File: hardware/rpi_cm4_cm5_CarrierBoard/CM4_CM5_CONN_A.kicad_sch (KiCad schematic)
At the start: 60 parts, among them J19 RPI_CMx_A, J6 M20-9990245, J7 2998TR, Q12 2N7002, U19 SN74LVC1G125DBVR, U21 MCP7940NT-I/MS, Y2 32.768kHz

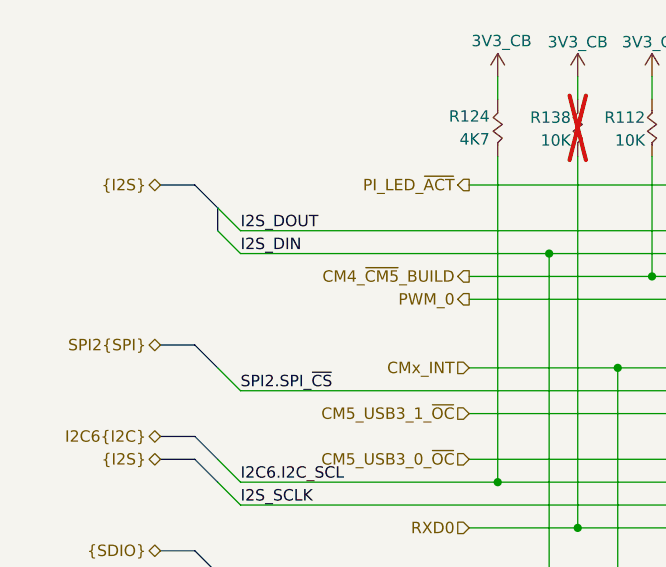
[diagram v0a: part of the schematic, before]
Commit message: Update preliminary placement, update DNP, regen BOM + Preliminary schematics
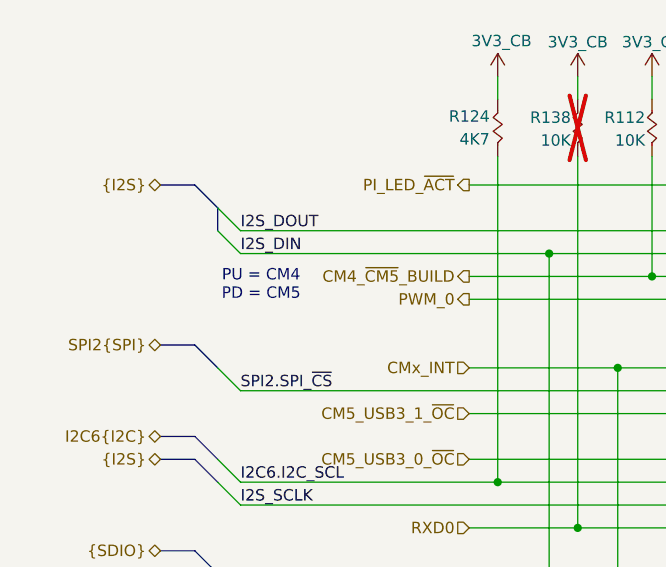
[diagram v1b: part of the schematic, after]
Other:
- note added: "PU = CM4 PD = CM5"
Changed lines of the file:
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@@
+		)
+	)
+	(text "PU = CM4\nPD = CM5"
+		(exclude_from_sim no)
+		(at 35.306 54.356 0)
+		(effects
+			(font
+				(size 1.27 1.27)
+				(color 255 153 0 1)
+			)
 		)
 	)

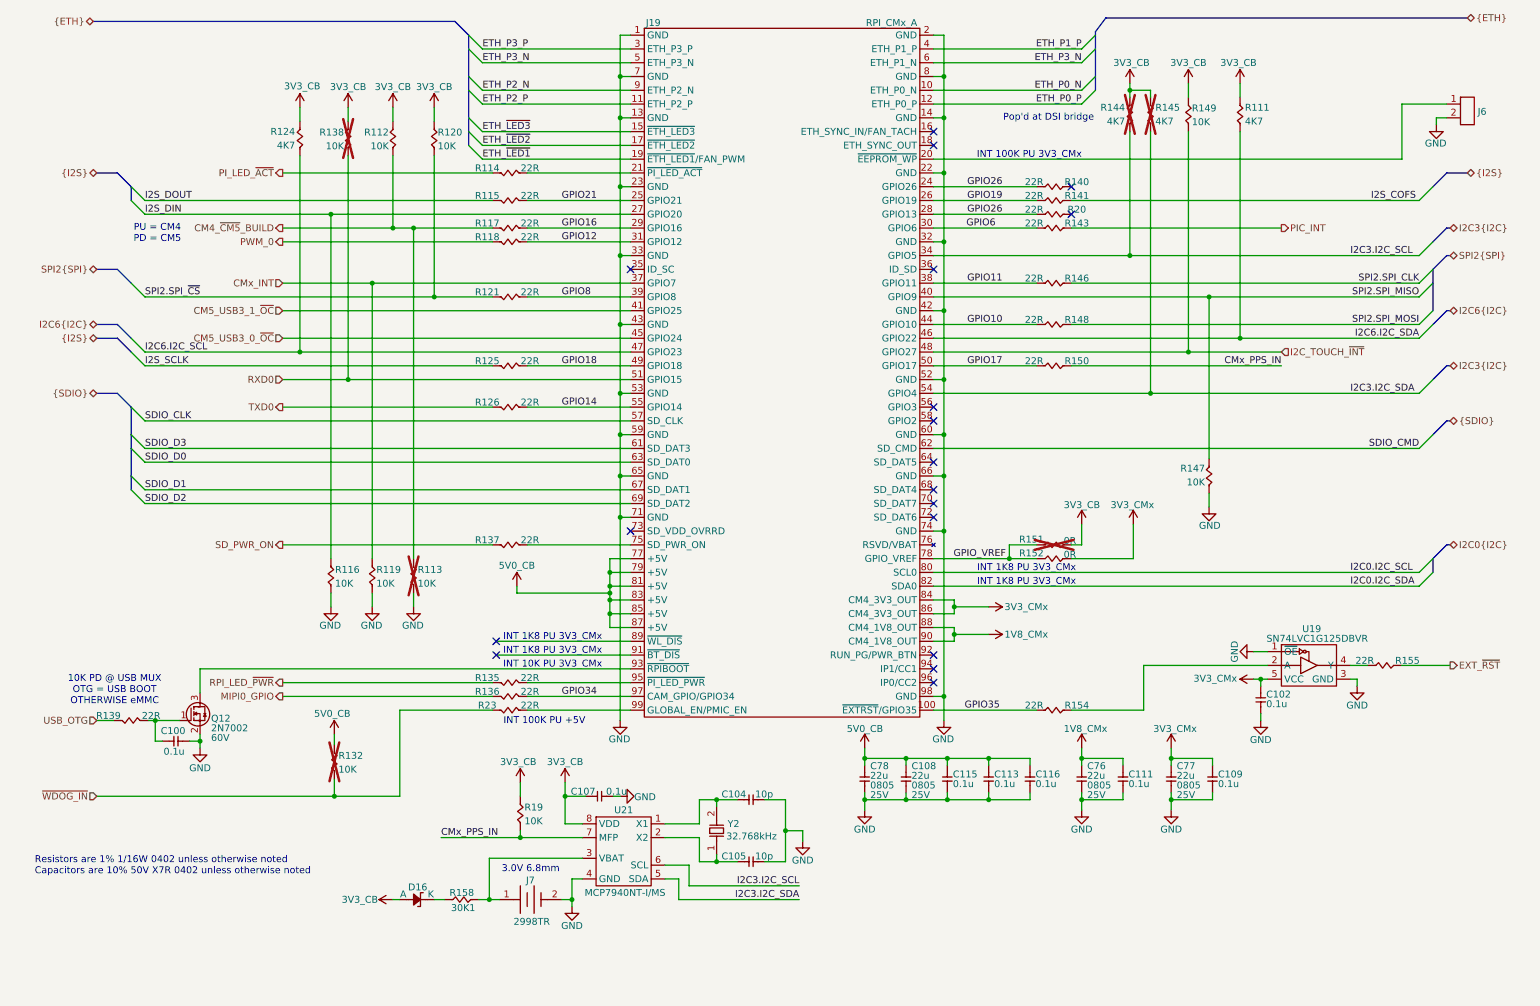
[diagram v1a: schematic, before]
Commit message: Update PCB design rules for outer layers differential pairs Update preliminary component placement Update schematics based on PCB placement & remove duplicata / unnecessary components Update design notes and power table
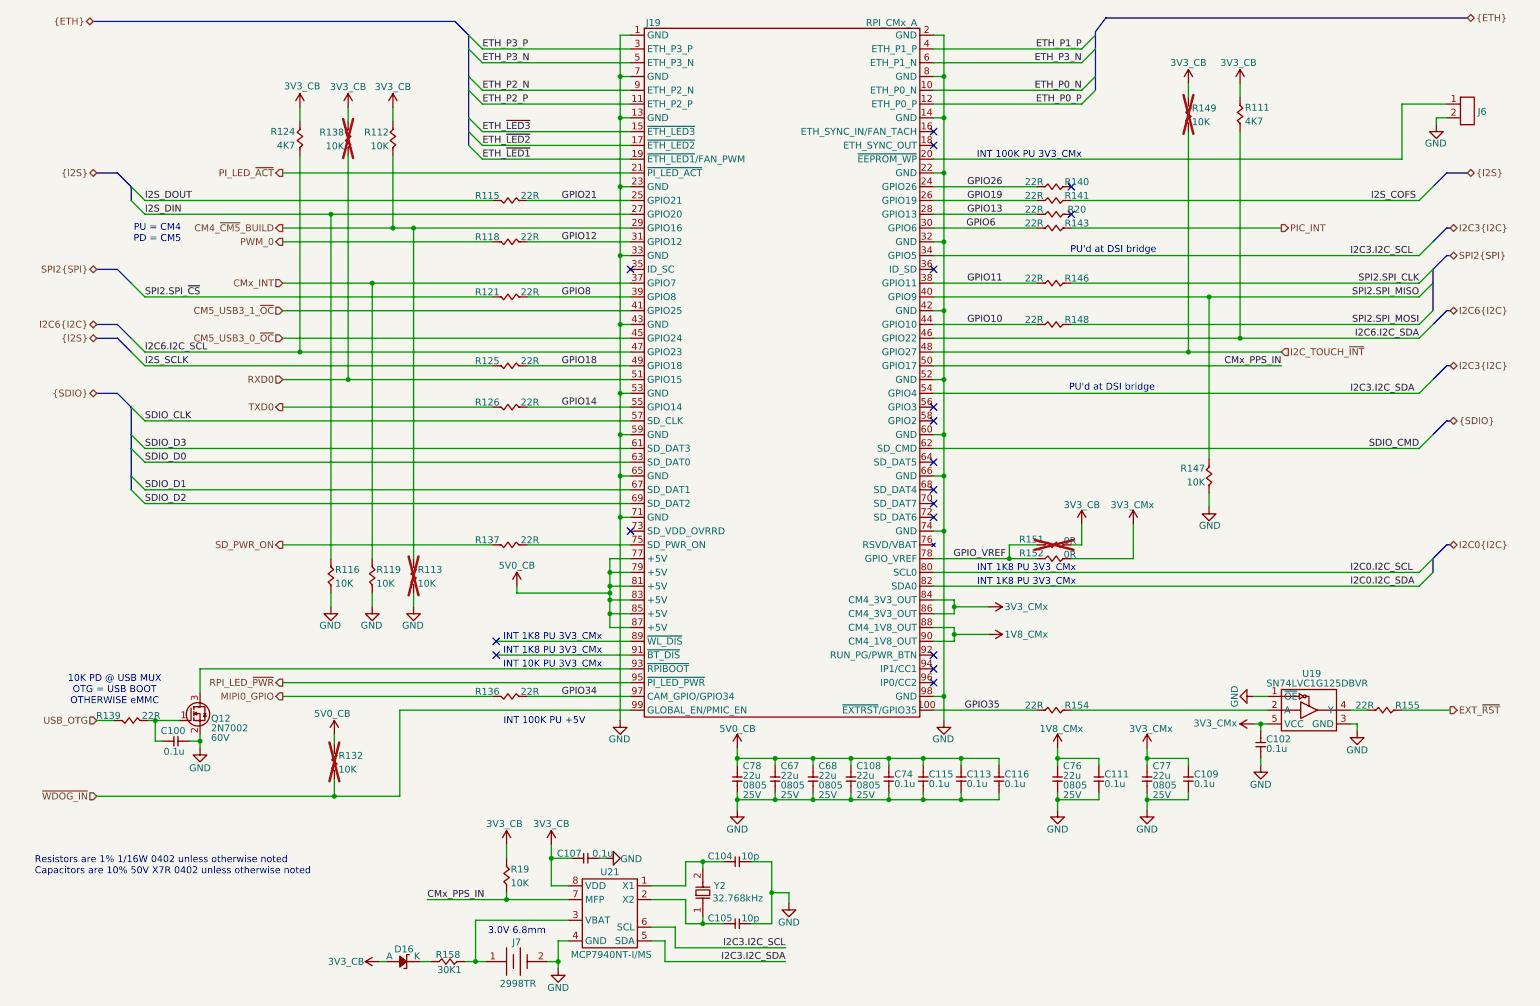
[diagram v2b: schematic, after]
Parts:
- removed R114, R117, R135, R150, R23: 22R, footprint:RES_0402, symbol KicadCompDb:Resistors/RES_SMT_00015
- removed R120: 10K, footprint:RES_0402, symbol KicadCompDb:Resistors/RES_SMT_00013
- removed R144, R145: 4K7, footprint:RES_0402, symbol KicadCompDb:Resistors/RES_SMT_00010
- added C67, C68: 22u, footprint:CAP_NONPOL_0805, symbol KicadCompDb:Capacitors/CAP_CER_SMT_00011
- added C74: 0.1u, footprint:CAP_NONPOL_0402, symbol KicadCompDb:Capacitors/CAP_CER_SMT_00001
- R149: now not fitted
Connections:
- net GPIO16 is gone; now on net CM4_~{CM5}_BUILD: J19.29 (GPIO16)
- net GPIO17 is gone; now on net CMx_PPS_IN: J19.50 (GPIO17)
- net 5V0_CB: now also C67.2, C68.2, C74.2
- net GND: now also C67.1, C68.1, C74.1
- net GPIO26: no longer J19.28 (GPIO13), R20.1
- net PI_LED_~{ACT}: now also J19.21 (~{PI_LED_ACT})
- net RPI_LED_~{PWR}: now also J19.95 (~{PI_LED_PWR})
- net ~{WDOG_IN}: now also J19.99 (GLOBAL_EN/PMIC_EN)
- new net GPIO13: J19.28 (GPIO13), R20.1
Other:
- note added: "PU'd at DSI bridge"
- note removed: "Pop'd at DSI bridge"
- moved on the sheet: C102, C104, C105, C107, C108, C109, C111, C113, C115, C116, C76, C77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

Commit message: Document stackup Few changes to schematic based on preliminary PCB placement Update PinMux based on preliminary PCB placement and component positions
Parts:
- removed R136: 22R, footprint:RES_0402, symbol KicadCompDb:Resistors/RES_SMT_00015
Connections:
- net GPIO34 is gone; now on net MIPI0_GPIO: J19.97 (CAM_GPIO/GPIO34)
- net CMx_PPS_IN renamed PPS_OUT
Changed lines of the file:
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@@
 	(title_block
 		(title "RPI CMx Carrier")
-		(date "2025-12-07")
+		(date "2026-01-22")
 		(rev "2.00-0A")
 		(comment 1 "Jean-Francois Bilodeau")
@@
 	(wire
 		(pts
-			(xy 103.505 139.7) (xy 122.555 139.7)
-		)
-		(stroke
-			(width 0)
-			(type default)
-		)
-	)
-	(wire
-		(pts
 			(xy 229.235 66.04) (xy 229.235 95.885)
 		)
@@
 	(wire
 		(pts
-			(xy 58.42 139.7) (xy 97.155 139.7)
+			(xy 58.42 139.7) (xy 122.555 139.7)
 		)
 		(stroke
@@
 		)
 	)
-	(label "CMx_PPS_IN"
-		(at 242.57 78.74 180)
-		(effects
-			(font
-				(size 1.27 1.27)
-			)
-			(justify right bottom)
-		)
-	)
 	(label "I2C0.I2C_SCL"
 		(at 255.27 116.84 0)
@@
 		)
 	)
-	(label "CMx_PPS_IN"
+	(label "PPS_OUT"
 		(at 85.09 177.165 0)
 		(effects
@@
 		)
 	)
+	(label "PPS_OUT"
+		(at 242.57 78.74 180)
+		(effects
+			(font
+				(size 1.27 1.27)
+			)
+			(justify right bottom)
+		)
+	)
 	(label "GPIO8"
 		(at 109.855 66.04 0)
@@
 		)
 	)
-	(label "GPIO34"
-		(at 109.855 139.7 0)
-		(effects
-			(font
-				(size 1.27 1.27)
-			)
-			(justify left bottom)
-		)
-	)
 	(label "I2C3.I2C_SCL"
 		(at 255.27 58.42 0)
@@
 		)
 	)
+	(hierarchical_label "PPS_OUT"
+		(shape output)
+		(at 85.09 177.165 180)
+		(effects
+			(font
+				(size 1.27 1.27)
+			)
+			(justify right)
+		)
+	)
 	(hierarchical_label "TXD0"
 		(shape output)
@@
 					(unit 1)
 				)
-			)
-		)
-	)
-	(symbol
-		(lib_id "KicadCompDb:Resistors/RES_SMT_00015")
-		(at 102.235 139.7 0)
-		(mirror y)
-		(unit 1)
-		(exclude_from_sim no)
-		(in_bom yes)
-		(on_board yes)
-		(dnp no)
-		(property "Reference" "R136"
-			(at 96.139 138.811 0)
-			(effects
-				(font
-					(size 1.27 1.27)
-				)
-			)
-		)
-		(property "Value" "22R"
-			(at 104.013 138.811 0)
-			(effects
-				(font
-					(size 1.27 1.27)
-				)
-			)
-		)
-		(property "Footprint" "footprint:RES_0402"
-			(at 101.727 161.798 0)
-			(effects
-				(font
-					(size 1.27 1.27)
-				)
-				(hide yes)
-			)
-		)
-		(property "Datasheet" "https://www.yageogroup.com/content/datasheet/asset/file/PYU-RC_GROUP_51_ROHS_L"
-			(at 102.235 139.7 0)
-			(effects
-				(font
-					(size 1.27 1.27)
-				)
-				(hide yes)
-			)
-		)
-		(property "Description" "RES 22 OHM 1% 1/16W 0402"
-			(at 100.457 149.606 0)
-			(effects
-				(font
-					(size 1.27 1.27)
-				)
-				(hide yes)
-			)
-		)
-		(property "Tolerance" "1%"
-			(at 101.981 160.02 0)
-			(effects
-				(font
-					(size 1.27 1.27)
-				)
-				(hide yes)
-			)
-		)
-		(property "Power" "1/16W"
-			(at 101.981 153.924 0)
-			(effects
-				(font
-					(size 1.27 1.27)
-				)
-				(hide yes)
-			)
-		)
-		(property "Package" "0402"
-			(at 102.235 155.956 0)
-			(effects
-				(font
-					(size 1.27 1.27)
-				)
-				(hide yes)
-			)
-		)
-		(property "Manufacturer" "YAGEO"
-			(at 101.981 157.988 0)
-			(effects
-				(font
-					(size 1.27 1.27)
-				)
-				(hide yes)
-			)
-		)
-		(property "Manufacturer Part Number" "RC0402FR-0722RL"
-			(at 101.981 147.574 0)
-			(effects
-				(font
-					(size 1.27 1.27)
-				)
-				(hide yes)
-			)
-		)
-		(property "Distributor" "DigiKey"
-			(at 102.235 145.542 0)
-			(effects
-				(font
-					(size 1.27 1.27)
-				)
-				(hide yes)
-			)
-		)
-		(property "Distributor Part Number" "311-22.0LRCT-ND"
-			(at 101.473 151.892 0)
-			(effects
-				(font
-					(size 1.27 1.27)
-				)
-				(hide yes)
-			)
-		)
-		(property "Temperature Coefficient" "±100ppm/°C"
-			(at 102.235 139.7 0)
-			(effects
-				(font
-					(size 1.27 1.27)
-				)
-				(hide yes)
-			)
-		)
-		(property "Operating Temperature" "-55°C ~ 155°C"
-			(at 101.473 164.084 0)
-			(effects
-				(font
-					(size 1.27 1.27)
-				)
-				(hide yes)
-			)
-		)
-		(property "Type" "RES SMT"
-			(at 102.235 139.7 0)
-			(show_name yes)
-			(effects
-				(font
-					(size 1.27 1.27)
-				)
-				(hide yes)
-			)
-		)
-		(property "Dimensions" "1.00mm x 0.50mm"
-			(at 102.235 139.7 0)
-			(show_name yes)
-			(effects
-				(font
-					(size 1.27 1.27)
-				)
-				(hide yes)
-			)
-		)
-		(pin "1"
-		)
-		(pin "2"
-		)
-		(instances
-			(project "rpi_cm4_cm5_CarrierBoard"
-				(path "/7dcdf741-90ca-4333-848c-806f4d64158e/b189385c-a3f2-4a0b-9ce6-a99cf7ff1f89"
-					(reference "R136")
-					(unit 1)
-				)

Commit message: Significant update in PCB layout; Completed preliminary high speed rules definition and fanout of differential pairs + GND vias. Started routing high speed signals Slight changes to Pinout based on component placement
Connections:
- net ETH_P3_N: no longer J19.6 (ETH_P1_N)
- new net ETH_P1_N: J19.6 (ETH_P1_N)
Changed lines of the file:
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@@
 		)
 	)
-	(label "ETH_P3_N"
+	(label "ETH_P1_N"
 		(at 205.74 22.86 180)
 		(effects

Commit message: Continue working on the layout. Completed most of power planes planning and pouring Completed all DiffPairs routing and length matching (preliminary)
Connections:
- net CM5_USB3_0_~{OC}: no longer names the net of J19.45 (GPIO24)
- net CM5_USB3_1_~{OC}: no longer names the net of J19.41 (GPIO25)
- no-connect marks 18 -> 20
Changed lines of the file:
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@@
 	)
 	(no_connect
+		(at 122.555 73.66)
+	)
+	(no_connect
 		(at 178.435 86.36)
 	)
@@
 	)
 	(no_connect
+		(at 122.555 68.58)
+	)
+	(no_connect
 		(at 178.435 134.62)
 	)
@@
 	(wire
 		(pts
-			(xy 58.42 73.66) (xy 122.555 73.66)
-		)
-		(stroke
-			(width 0)
-			(type default)
-		)
-	)
-	(wire
-		(pts
 			(xy 103.505 66.04) (xy 122.555 66.04)
 		)
@@
 	(wire
 		(pts
-			(xy 58.42 68.58) (xy 122.555 68.58)
-		)
-		(stroke
-			(width 0)
-			(type default)
-		)
-	)
-	(wire
-		(pts
 			(xy 149.225 152.4) (xy 149.225 151.13)
 		)
@@
 		)
 	)
-	(hierarchical_label "CM5_USB3_0_~{OC}"
-		(shape input)
-		(at 58.42 73.66 180)
-		(effects
-			(font
-				(size 1.27 1.27)
-			)
-			(justify right)
-		)
-	)
 	(hierarchical_label "SPI2{SPI}"
 		(shape bidirectional)
@@
 		(effects
 			(font
-				(size 1.27 1.27)
-			)
-			(justify right)
-		)
-	)
-	(hierarchical_label "CM5_USB3_1_~{OC}"
-		(shape input)
-		(at 58.42 68.58 180)
-		(effects
-			(font

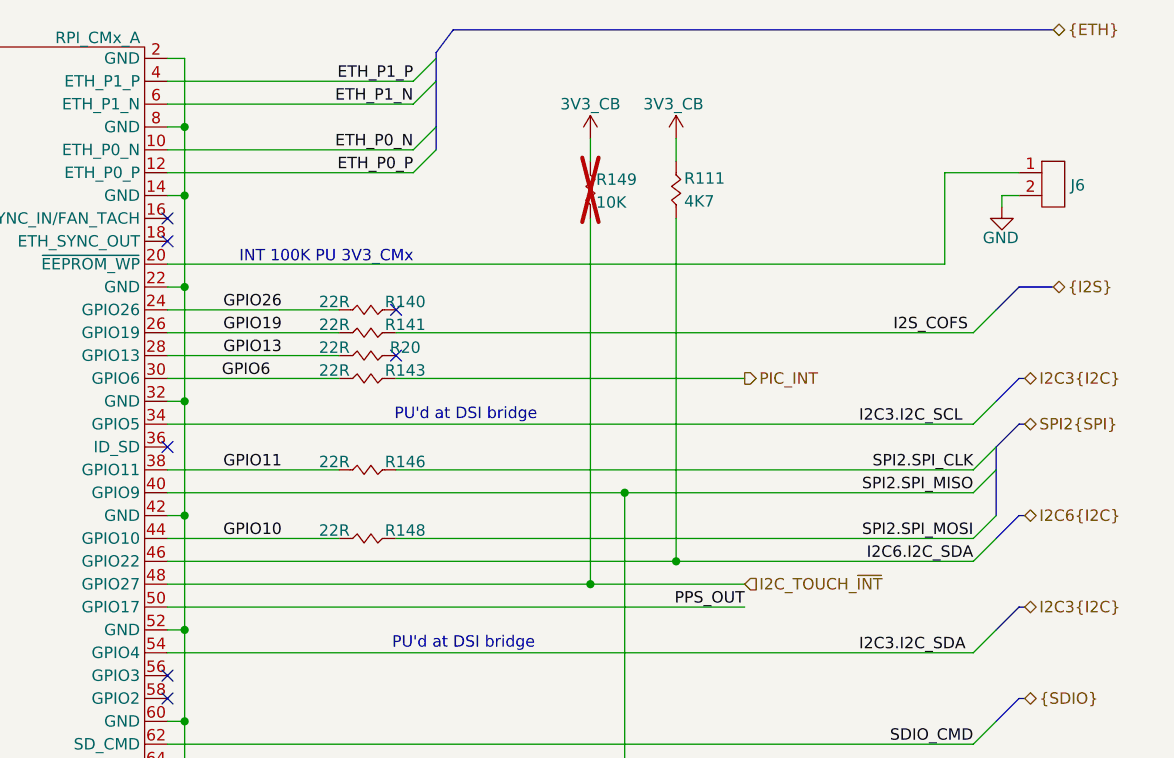
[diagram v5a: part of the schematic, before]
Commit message: Significant update Stackup changed from 6 to 8 layers Changed design notes accordingly Re-routed all differential pairs and length match / skew match Fanout critical signals away from dense areas 95% routing completed
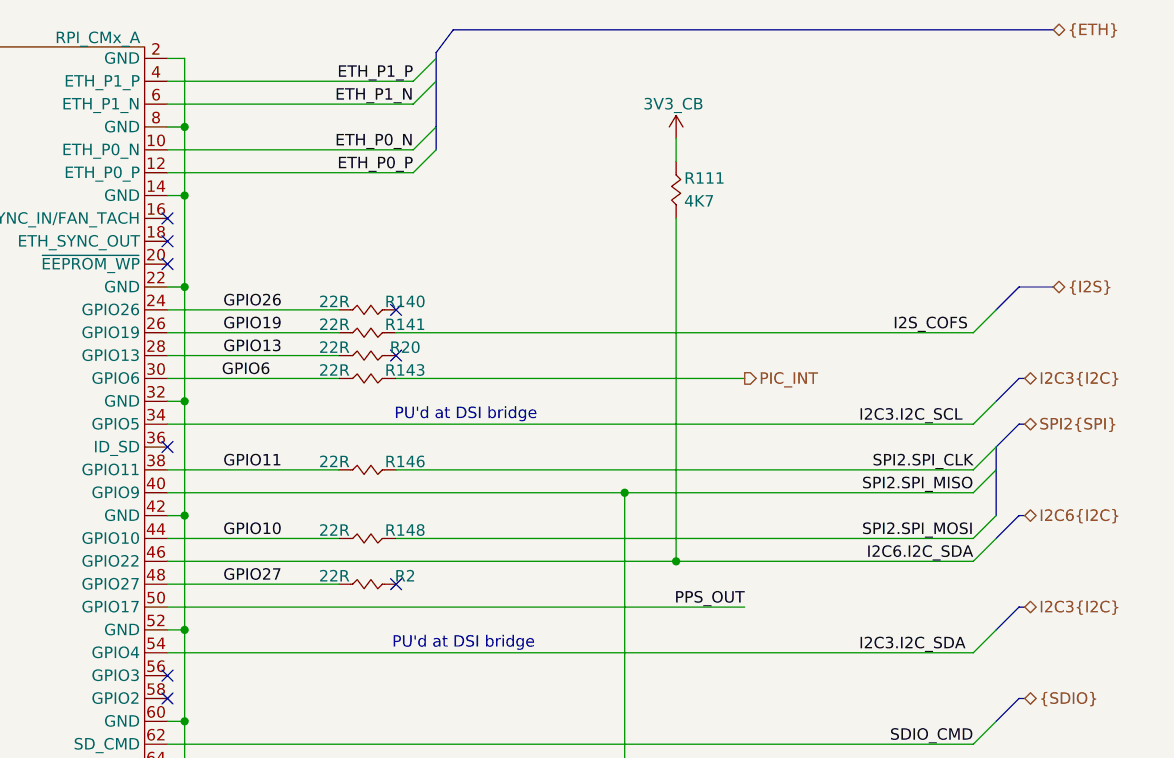
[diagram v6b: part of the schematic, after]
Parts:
- removed J6: M20-9990245, footprint:HEADER_2P_2_54MM, symbol KicadCompDb:Connector/CONN_00003
- removed R149: 10K, footprint:RES_0402, symbol KicadCompDb:Resistors/RES_SMT_00013
- added R2: 22R, footprint:RES_0402, symbol KicadCompDb:Resistors/RES_SMT_00015
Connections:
- net I2C_TOUCH_~{INT} renamed GPIO27
- net GPIO27: now also R2.1
- no-connect marks 20 -> 22
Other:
- note removed: "INT 100K PU 3V3_CMx"
